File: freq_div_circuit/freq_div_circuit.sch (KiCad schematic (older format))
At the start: 18 parts, among them P1 BNC, P2 BNC, U1 TL071, U2 MAX1044, U3 MCP6021, U4 7805, U5 7905

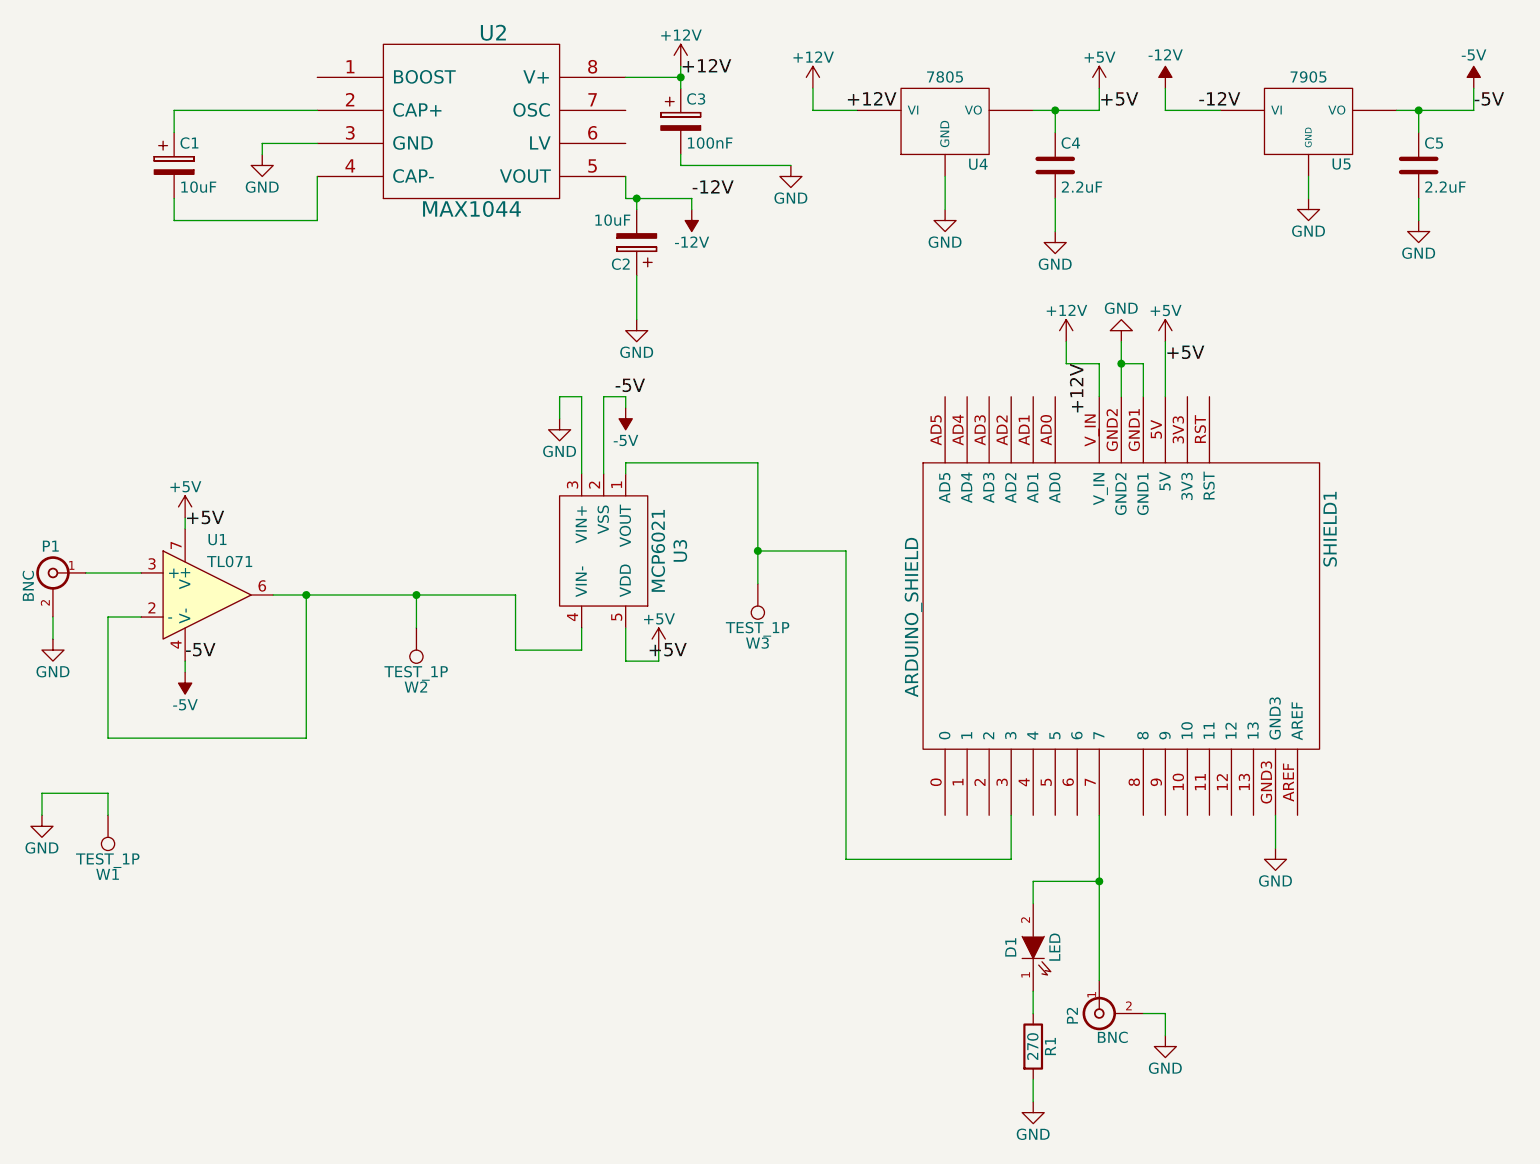
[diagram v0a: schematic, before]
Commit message: updating schematic with tl071cp
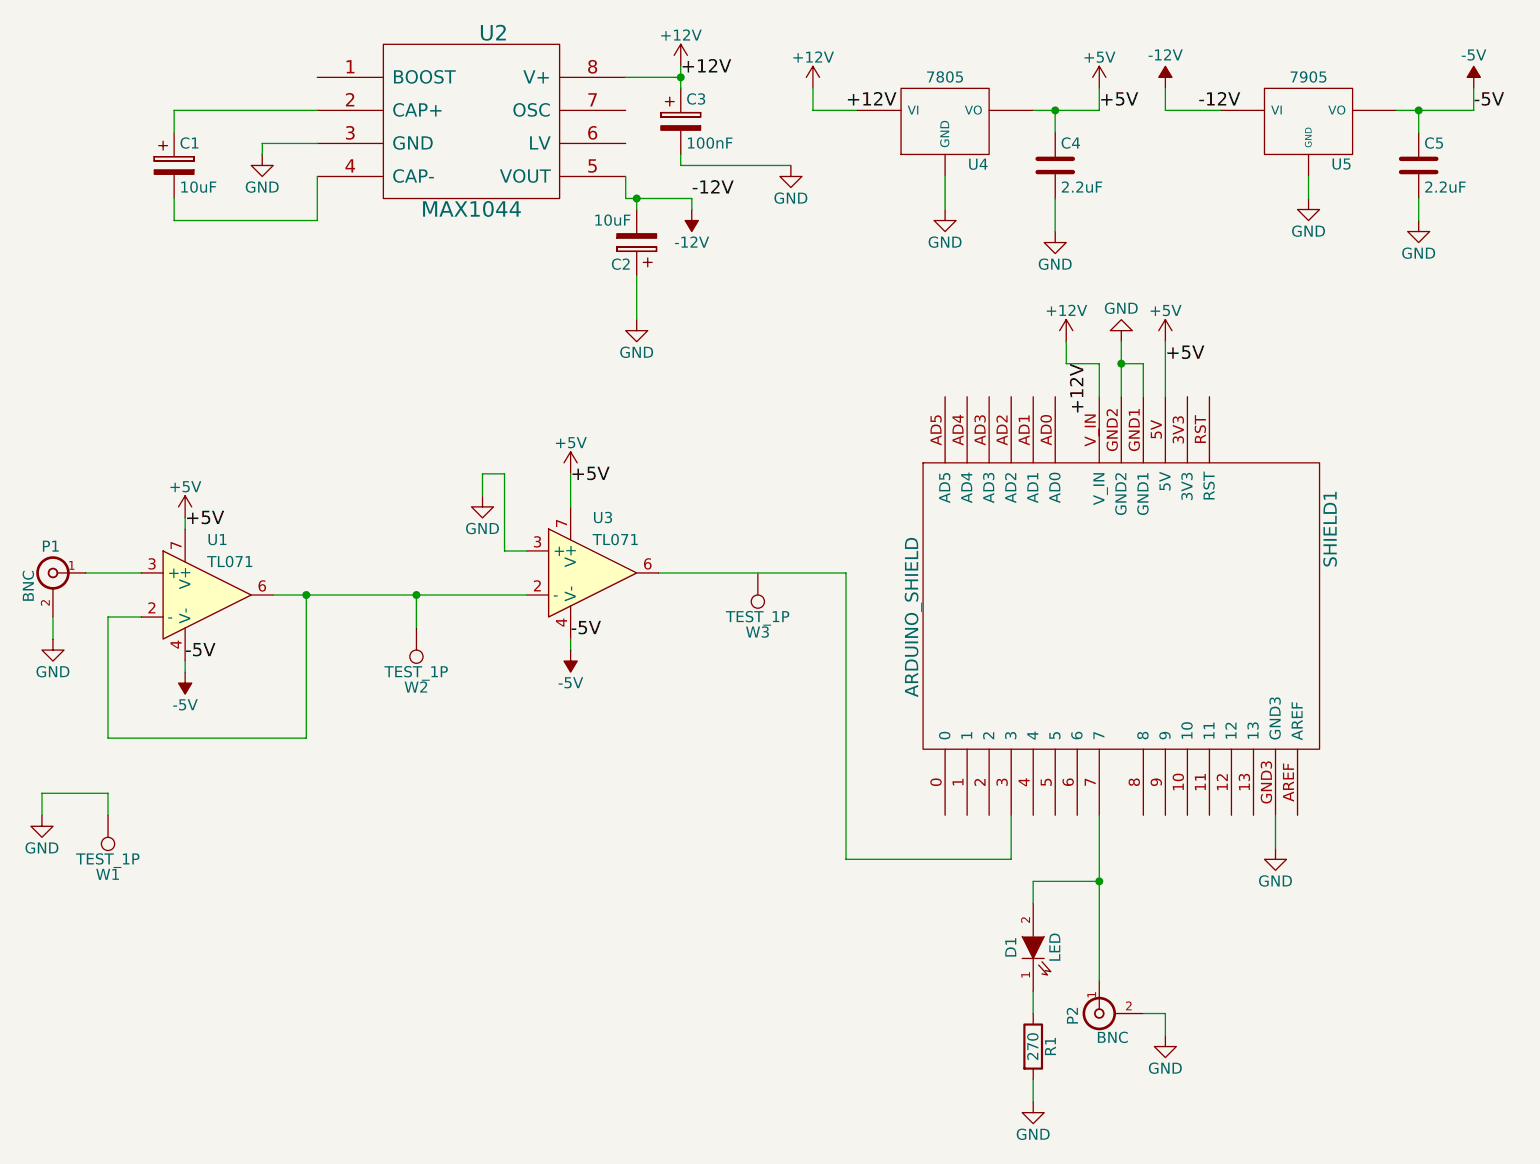
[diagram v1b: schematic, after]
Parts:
- removed U3: MCP6021, Housings_DIP:DIP-8_W7.62mm, symbol MCP6021
- added U3: TL071, symbol TL071
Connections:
- net +5V: now also U3.7 (V+)
- net -5V: now also U3.4 (V-)
- net GND: now also U3.3 (+)
- net at U1.2 (-), U1.6, W2.1: now also U3.2 (-)
- net at SHIELD1.3: now also U3.6; no longer W3.1
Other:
- moved on the sheet: W3
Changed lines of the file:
@@
 $EndComp
 $Comp
-L -5V #PWR7
+L -5V #PWR8
 U 1 1 59C3BA95
-P 5600 2800
-F 0 "#PWR7" H 5600 2900 50  0001 C CNN
-F 1 "-5V" H 5600 2950 50  0000 C CNN
-F 2 "" H 5600 2800 50  0000 C CNN
-F 3 "" H 5600 2800 50  0000 C CNN
-	1    5600 2800
-	-1   0    0    1
-$EndComp
-$Comp
-L +5V #PWR01
+P 5350 3900
+F 0 "#PWR8" H 5350 4000 50  0001 C CNN
+F 1 "-5V" H 5350 4050 50  0000 C CNN
+F 2 "" H 5350 3900 50  0000 C CNN
+F 3 "" H 5350 3900 50  0000 C CNN
+	1    5350 3900
+	-1   0    0    1
+$EndComp
+$Comp
+L +5V #PWR3
 U 1 1 59C3BAB7
 P 3600 3300
-F 0 "#PWR01" H 3600 3150 50  0001 C CNN
+F 0 "#PWR3" H 3600 3150 50  0001 C CNN
 F 1 "+5V" H 3600 3440 50  0000 C CNN
 F 2 "" H 3600 3300 50  0000 C CNN
@@
 $EndComp
 $Comp
-L +5V #PWR02
+L +5V #PWR7
 U 1 1 59C3BAD9
-P 5750 3900
-F 0 "#PWR02" H 5750 3750 50  0001 C CNN
-F 1 "+5V" H 5750 4040 50  0000 C CNN
-F 2 "" H 5750 3900 50  0000 C CNN
-F 3 "" H 5750 3900 50  0000 C CNN
-	1    5750 3900
-	1    0    0    -1
-$EndComp
-$Comp
-L +5V #PWR03
+P 5350 3100
+F 0 "#PWR7" H 5350 2950 50  0001 C CNN
+F 1 "+5V" H 5350 3240 50  0000 C CNN
+F 2 "" H 5350 3100 50  0000 C CNN
+F 3 "" H 5350 3100 50  0000 C CNN
+	1    5350 3100
+	1    0    0    -1
+$EndComp
+$Comp
+L +5V #PWR21
 U 1 1 59C3BB22
 P 8050 2500
-F 0 "#PWR03" H 8050 2350 50  0001 C CNN
+F 0 "#PWR21" H 8050 2350 50  0001 C CNN
 F 1 "+5V" H 8050 2640 50  0000 C CNN
 F 2 "" H 8050 2500 50  0000 C CNN
@@
 	8050 2750 8050 2500
 $Comp
-L GND #PWR04
+L GND #PWR19
 U 1 1 59C3BB47
 P 7850 2500
-F 0 "#PWR04" H 7850 2250 50  0001 C CNN
+F 0 "#PWR19" H 7850 2250 50  0001 C CNN
 F 1 "GND" H 7850 2350 50  0000 C CNN
 F 2 "" H 7850 2500 50  0000 C CNN
@@
 Connection ~ 7850 2600
 $Comp
-L GND #PWR05
+L GND #PWR23
 U 1 1 59C3BBBC
 P 8550 4800
-F 0 "#PWR05" H 8550 4550 50  0001 C CNN
+F 0 "#PWR23" H 8550 4550 50  0001 C CNN
 F 1 "GND" H 8550 4650 50  0000 C CNN
 F 2 "" H 8550 4800 50  0000 C CNN
@@
 	7750 4650 7750 5400
 $Comp
-L GND #PWR06
+L GND #PWR22
 U 1 1 59C3BC7A
 P 8050 5650
-F 0 "#PWR06" H 8050 5400 50  0001 C CNN
+F 0 "#PWR22" H 8050 5400 50  0001 C CNN
 F 1 "GND" H 8050 5500 50  0000 C CNN
 F 2 "" H 8050 5650 50  0000 C CNN
@@
 	8050 5550 8050 5650
 $Comp
-L GND #PWR07
+L GND #PWR2
 U 1 1 59C3BCDD
 P 3000 3850
-F 0 "#PWR07" H 3000 3600 50  0001 C CNN
+F 0 "#PWR2" H 3000 3600 50  0001 C CNN
 F 1 "GND" H 3000 3700 50  0000 C CNN
 F 2 "" H 3000 3850 50  0000 C CNN
@@
 $EndComp
 $Comp
-L GND #PWR08
+L GND #PWR14
 U 1 1 59C3BEC4
 P 7050 1900
-F 0 "#PWR08" H 7050 1650 50  0001 C CNN
+F 0 "#PWR14" H 7050 1650 50  0001 C CNN
 F 1 "GND" H 7050 1750 50  0000 C CNN
 F 2 "" H 7050 1900 50  0000 C CNN
@@
 $EndComp
 Wire Wire Line
-	7750 1350 7750 1450
-Wire Wire Line
-	7750 1450 7450 1450
+	7750 1450 7750 1350
+Wire Wire Line
+	7450 1450 7750 1450
 Wire Wire Line
 	6450 1350 6450 1450
@@
 	3600 3300 3600 3350
 $Comp
-L +5V #PWR09
+L +5V #PWR18
 U 1 1 59C3C09F
 P 7750 1350
-F 0 "#PWR09" H 7750 1200 50  0001 C CNN
+F 0 "#PWR18" H 7750 1200 50  0001 C CNN
 F 1 "+5V" H 7750 1490 50  0000 C CNN
 F 2 "" H 7750 1350 50  0000 C CNN
@@
 	9100 1450 9450 1450
 $Comp
-L GND #PWR010
+L GND #PWR24
 U 1 1 59C3C7F7
 P 8700 1850
-F 0 "#PWR010" H 8700 1600 50  0001 C CNN
+F 0 "#PWR24" H 8700 1600 50  0001 C CNN
 F 1 "GND" H 8700 1700 50  0000 C CNN
 F 2 "" H 8700 1850 50  0000 C CNN
@@
 $EndComp
 $Comp
-L +12V #PWR011
+L +12V #PWR13
 U 1 1 59C3C885
 P 6450 1350
-F 0 "#PWR011" H 6450 1200 50  0001 C CNN
+F 0 "#PWR13" H 6450 1200 50  0001 C CNN
 F 1 "+12V" H 6450 1490 50  0000 C CNN
 F 2 "" H 6450 1350 50  0000 C CNN
@@
 $EndComp
 $Comp
-L GND #PWR012
+L GND #PWR25
 U 1 1 59C3C8EC
 P 9200 1950
-F 0 "#PWR012" H 9200 1700 50  0001 C CNN
+F 0 "#PWR25" H 9200 1700 50  0001 C CNN
 F 1 "GND" H 9200 1800 50  0000 C CNN
 F 2 "" H 9200 1950 50  0000 C CNN
@@
 L TEST_1P W3
 U 1 1 59C3CAA1
-P 6200 3600
-F 0 "W3" H 6200 3870 50  0000 C CNN
-F 1 "TEST_1P" H 6200 3800 50  0000 C CNN
-F 2 "Connect:PINTST" H 6400 3600 50  0001 C CNN
-F 3 "" H 6400 3600 50  0000 C CNN
-	1    6200 3600
+P 6200 3550
+F 0 "W3" H 6200 3820 50  0000 C CNN
+F 1 "TEST_1P" H 6200 3750 50  0000 C CNN
+F 2 "Connect:PINTST" H 6400 3550 50  0001 C CNN
+F 3 "" H 6400 3550 50  0000 C CNN
+	1    6200 3550
 	-1   0    0    1
 $EndComp
@@
 $EndComp
 $Comp
-L GND #PWR013
+L GND #PWR1
 U 1 1 59C3CB7D
 P 2950 4650
-F 0 "#PWR013" H 2950 4400 50  0001 C CNN
+F 0 "#PWR1" H 2950 4400 50  0001 C CNN
 F 1 "GND" H 2950 4500 50  0000 C CNN
 F 2 "" H 2950 4650 50  0000 C CNN
@@
 $EndComp
 $Comp
-L GND #PWR014
+L GND #PWR5
 U 1 1 59C3CEC0
 P 3950 1650
-F 0 "#PWR014" H 3950 1400 50  0001 C CNN
+F 0 "#PWR5" H 3950 1400 50  0001 C CNN
 F 1 "GND" H 3950 1500 50  0000 C CNN
 F 2 "" H 3950 1650 50  0000 C CNN
@@
 	3950 1600 4200 1600
 $Comp
-L +12V #PWR015
+L +12V #PWR10
 U 1 1 59C3CFE4
 P 5850 1250
-F 0 "#PWR015" H 5850 1100 50  0001 C CNN
+F 0 "#PWR10" H 5850 1100 50  0001 C CNN
 F 1 "+12V" H 5850 1390 50  0000 C CNN
 F 2 "" H 5850 1250 50  0000 C CNN
@@
 	5850 1250 5850 1350
 $Comp
-L -12V #PWR12
+L -12V #PWR11
 U 1 1 59C3D054
 P 5900 1900
-F 0 "#PWR12" H 5900 2000 50  0001 C CNN
+F 0 "#PWR11" H 5900 2000 50  0001 C CNN
 F 1 "-12V" H 5900 2050 50  0000 C CNN
 F 2 "" H 5900 1900 50  0000 C CNN
@@
 $EndComp
 $Comp
-L GND #PWR016
+L GND #PWR9
 U 1 1 59C3D107
 P 5650 2400
-F 0 "#PWR016" H 5650 2150 50  0001 C CNN
+F 0 "#PWR9" H 5650 2150 50  0001 C CNN
 F 1 "GND" H 5650 2250 50  0000 C CNN
 F 2 "" H 5650 2400 50  0000 C CNN
@@
 $EndComp
 $Comp
-L GND #PWR017
+L GND #PWR12
 U 1 1 59C3D372
 P 6350 1700
-F 0 "#PWR017" H 6350 1450 50  0001 C CNN
+F 0 "#PWR12" H 6350 1450 50  0001 C CNN
 F 1 "GND" H 6350 1550 50  0000 C CNN
 F 2 "" H 6350 1700 50  0000 C CNN
@@
 	3250 4300 4150 4300
 Wire Wire Line
-	4000 3650 5100 3650
-Wire Wire Line
 	4150 4300 4150 3650
-Connection ~ 4150 3650
-Wire Wire Line
-	6600 3450 6600 4850
 Wire Wire Line
 	6600 4850 7350 4850
@@
 	7350 4850 7350 4650
 Wire Wire Line
-	6200 3050 6200 3600
-Connection ~ 6200 3450
-Wire Wire Line
-	4650 3800 4650 3650
-Connection ~ 4650 3650
-$Comp
-L MCP6021 U3
-U 1 1 59C3E65E
-P 5500 3450
-F 0 "U3" H 5500 3800 60  0000 C CNN
-F 1 "MCP6021" H 5500 3700 60  0000 C CNN
-F 2 "Housings_DIP:DIP-8_W7.62mm" H 5500 3450 60  0001 C CNN
-F 3 "" H 5500 3450 60  0000 C CNN
-	1    5500 3450
-	0    1    1    0
-$EndComp
-Wire Wire Line
-	5600 3800 5600 3950
-Wire Wire Line
-	5600 3950 5750 3950
-Wire Wire Line
-	5750 3950 5750 3900
-Wire Wire Line
-	5500 3100 5500 2750
-Wire Wire Line
-	5500 2750 5600 2750
-Wire Wire Line
-	5600 2750 5600 2800
-$Comp
-L GND #PWR018
+	4650 3650 4650 3800
+Wire Wire Line
+	5350 3850 5350 3900
+$Comp
+L GND #PWR6
 U 1 1 59C3EAE6
-P 5300 2850
-F 0 "#PWR018" H 5300 2600 50  0001 C CNN
-F 1 "GND" H 5300 2700 50  0000 C CNN
-F 2 "" H 5300 2850 50  0000 C CNN
-F 3 "" H 5300 2850 50  0000 C CNN
-	1    5300 2850
-	1    0    0    -1
-$EndComp
-Wire Wire Line
-	5400 3100 5400 2750
-Wire Wire Line
-	5400 2750 5300 2750
-Wire Wire Line
-	5300 2750 5300 2850
-Wire Wire Line
-	5600 3100 5600 3050
-Wire Wire Line
-	5600 3050 6200 3050
-Wire Wire Line
-	6200 3450 6600 3450
-Wire Wire Line
-	5100 3650 5100 3900
-Wire Wire Line
-	5100 3900 5400 3900
-Wire Wire Line
-	5400 3900 5400 3800
+P 4950 3200
+F 0 "#PWR6" H 4950 2950 50  0001 C CNN
+F 1 "GND" H 4950 3050 50  0000 C CNN
+F 2 "" H 4950 3200 50  0000 C CNN
+F 3 "" H 4950 3200 50  0000 C CNN
+	1    4950 3200
+	1    0    0    -1
+$EndComp
+Wire Wire Line
+	5050 3450 5050 3100
+Wire Wire Line
+	5050 3100 4950 3100
+Wire Wire Line
+	4950 3100 4950 3200
 $Comp
 L LED D1
@@
 	7450 5850 7450 5950
 $Comp
-L GND #PWR019
+L GND #PWR15
 U 1 1 59C3F192
 P 7450 5950
-F 0 "#PWR019" H 7450 5700 50  0001 C CNN
+F 0 "#PWR15" H 7450 5700 50  0001 C CNN
 F 1 "GND" H 7450 5800 50  0000 C CNN
 F 2 "" H 7450 5950 50  0000 C CNN
@@
 $EndComp
 $Comp
-L +12V #PWR020
+L +12V #PWR17
 U 1 1 59C3FA24
 P 7600 2500
-F 0 "#PWR020" H 7600 2350 50  0001 C CNN
+F 0 "#PWR17" H 7600 2350 50  0001 C CNN
 F 1 "+12V" H 7600 2640 50  0000 C CNN
 F 2 "" H 7600 2500 50  0000 C CNN
@@
 	7550 1850 7550 2000
 $Comp
-L GND #PWR021
+L GND #PWR16
 U 1 1 59C403C4
 P 7550 2000
-F 0 "#PWR021" H 7550 1750 50  0001 C CNN
+F 0 "#PWR16" H 7550 1750 50  0001 C CNN
 F 1 "GND" H 7550 1850 50  0000 C CNN
 F 2 "" H 7550 2000 50  0000 C CNN
@@
 Wire Wire Line
 	3000 3750 3000 3850
-Text Label 5550 2750 0    60   ~ 0
+Text Label 5350 3850 0    60   ~ 0
 -5V
-Text Label 5700 3950 0    60   ~ 0
+Text Label 5350 3150 0    60   ~ 0
 +5V
 Text Label 3600 3950 0    60   ~ 0
@@
 	5850 1700 5850 1650
 Connection ~ 5850 1300
+$Comp
+L TL071 U3
+U 1 1 59F7851E
+P 5450 3550
+F 0 "U3" H 5450 3800 50  0000 L CNN
+F 1 "TL071" H 5450 3700 50  0000 L CNN
+F 2 "" H 5500 3750 50  0000 C CNN
+F 3 "" H 5450 3800 50  0000 C CNN
+	1    5450 3550
+	1    0    0    -1
+$EndComp
+Wire Wire Line
+	4000 3650 5150 3650
+Connection ~ 4150 3650
+Connection ~ 4650 3650
+Wire Wire Line
+	5050 3450 5150 3450
+Wire Wire Line
+	5350 3250 5350 3100
+Wire Wire Line
+	6600 4850 6600 3550
+Wire Wire Line
+	6600 3550 5750 3550
 $EndSCHEMATC
